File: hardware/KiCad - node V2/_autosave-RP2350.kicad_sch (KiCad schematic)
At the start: 91 parts, among them J3 USB_C_Receptacle_USB2.0_14P, SW1 BOOTSEL, U1 RP2350A, U2 THVD1450D, U3 ADXL355BEZ, U4 TPS2121RUXR, U5 USBLC6-2SC6, U6 TLV75733PDBV, U7 W25Q128JVS, U8 TPS7A20xxxDBV

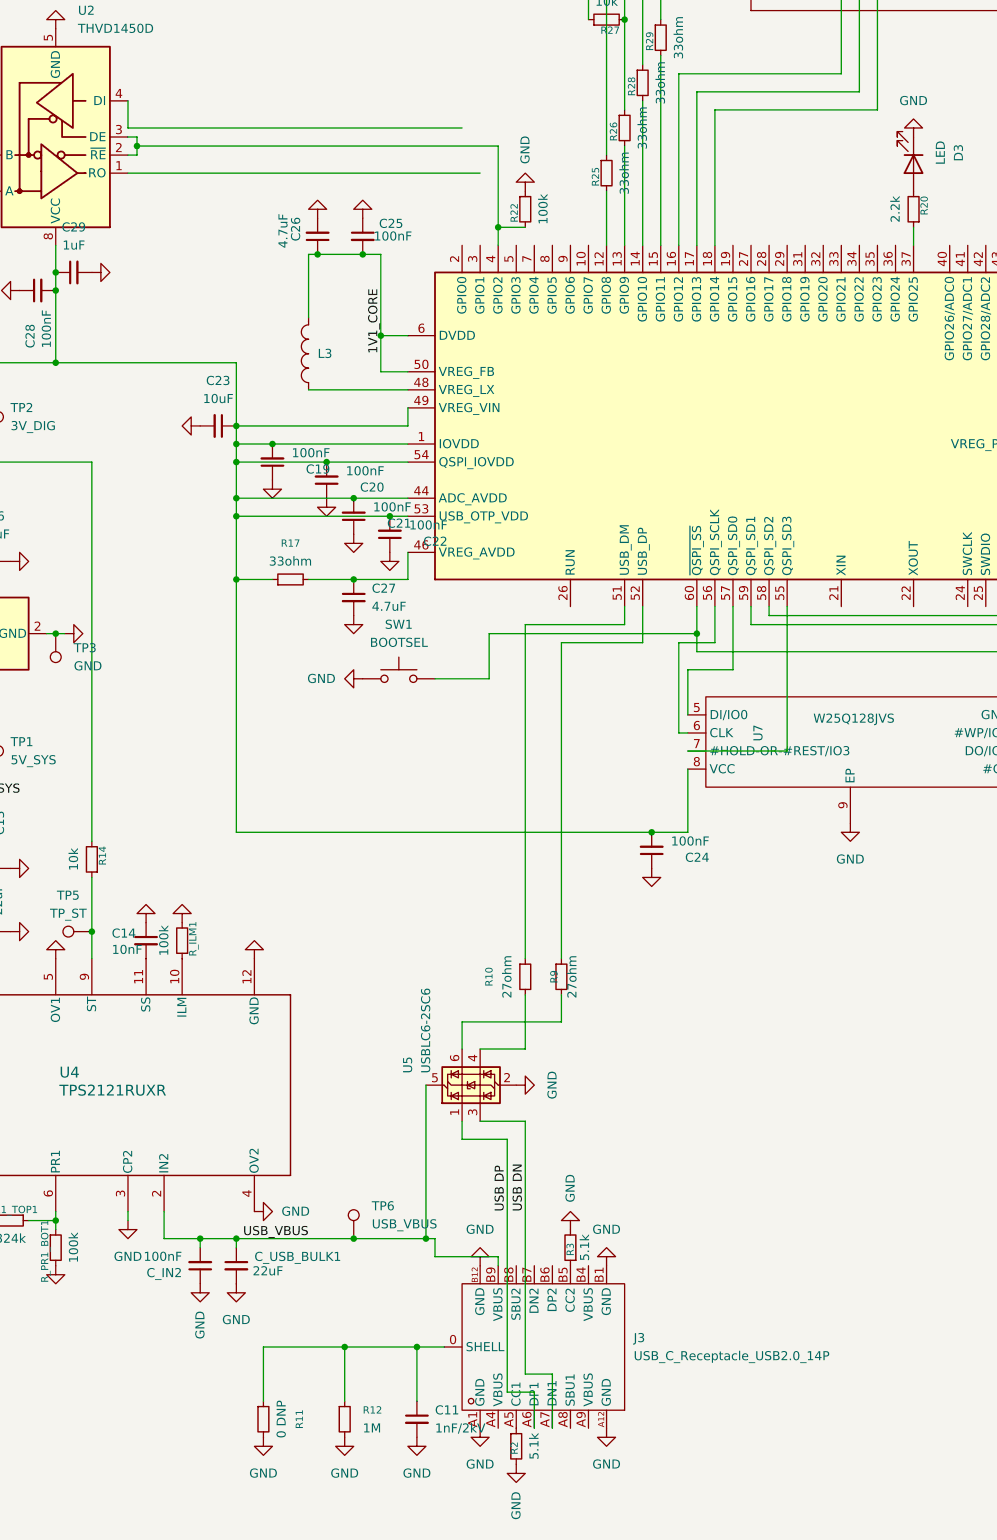
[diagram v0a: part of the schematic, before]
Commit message: hardware: 3v3_dig, 1vcore
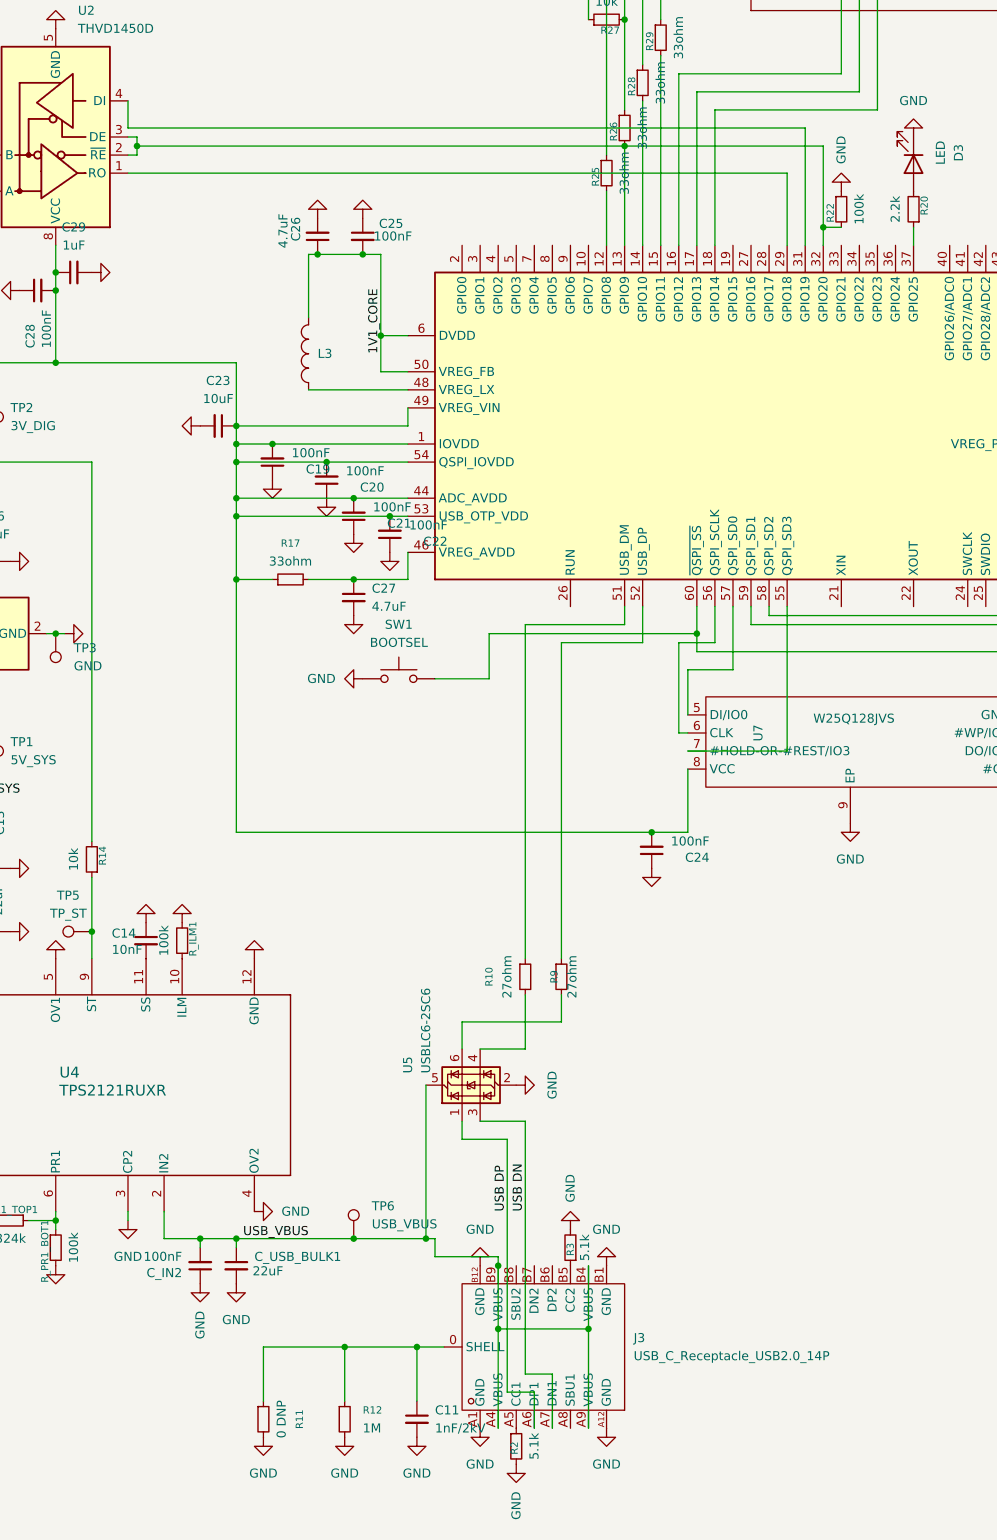
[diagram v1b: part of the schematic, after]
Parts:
- C19, C20, C21, C22, C25: footprint Capacitor_SMD:C_0603_1608Metric -> Capacitor_SMD:C_0402_1005Metric
- C23, C26: footprint Capacitor_SMD:C_0805_2012Metric -> Capacitor_SMD:C_0603_1608Metric
- R17: footprint Resistor_SMD:R_0201_0603Metric -> Resistor_SMD:R_0402_1005Metric
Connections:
- net USB_VBUS: now also J3.A4 (VBUS), J3.A9 (VBUS), J3.B4 (VBUS)
- net at U2.1 (RO): now also U1.29 (GPIO18)
- net at R22.2, U2.2 (~{RE}), U2.3 (DE): now also R26.2, U1.13 (GPIO9), U1.32 (GPIO20); no longer U1.4 (GPIO2)
- net at U2.4 (DI): now also U1.31 (GPIO19)
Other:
- moved on the sheet: R22
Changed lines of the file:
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@@
 	)
 	(junction
+		(at 186.69 241.3)
+		(diameter 0)
+		(color 0 0 0 0)
+	)
+	(junction
 		(at 137.16 228.6)
 		(diameter 0)
@@
 	)
 	(junction
+		(at 173.99 232.41)
+		(diameter 0)
+		(color 0 0 0 0)
+	)
+	(junction
+		(at 219.71 86.36)
+		(diameter 0)
+		(color 0 0 0 0)
+	)
+	(junction
 		(at 100.33 113.03)
 		(diameter 0)
@@
 	)
 	(junction
-		(at 173.99 86.36)
-		(diameter 0)
-		(color 0 0 0 0)
-	)
-	(junction
 		(at 66.04 34.29)
 		(diameter 0)
@@
 	)
 	(junction
+		(at 173.99 241.3)
+		(diameter 0)
+		(color 0 0 0 0)
+	)
+	(junction
 		(at 46.99 237.49)
 		(diameter 0)
@@
 	)
 	(junction
+		(at 191.77 74.93)
+		(diameter 0)
+		(color 0 0 0 0)
+	)
+	(junction
 		(at 137.16 127)
 		(diameter 0)
@@
 	(wire
 		(pts
+			(xy 186.69 255.27) (xy 186.69 241.3)
+		)
+		(stroke
+			(width 0)
+			(type default)
+		)
+	)
+	(wire
+		(pts
 			(xy 196.85 31.75) (xy 196.85 34.29)
 		)
@@
 	(wire
 		(pts
+			(xy 219.71 74.93) (xy 219.71 86.36)
+		)
+		(stroke
+			(width 0)
+			(type default)
+		)
+	)
+	(wire
+		(pts
 			(xy 194.31 88.9) (xy 194.31 68.58)
 		)
@@
 	(wire
 		(pts
+			(xy 219.71 86.36) (xy 222.25 86.36)
+		)
+		(stroke
+			(width 0)
+			(type default)
+		)
+	)
+	(wire
+		(pts
+			(xy 214.63 78.74) (xy 214.63 88.9)
+		)
+		(stroke
+			(width 0)
+			(type default)
+		)
+	)
+	(wire
+		(pts
 			(xy 201.93 40.64) (xy 198.12 40.64)
 		)
@@
 	(wire
 		(pts
+			(xy 186.69 232.41) (xy 186.69 241.3)
+		)
+		(stroke
+			(width 0)
+			(type default)
+		)
+	)
+	(wire
+		(pts
 			(xy 123.19 76.2) (xy 121.92 76.2)
 		)
@@
 	(wire
 		(pts
+			(xy 191.77 74.93) (xy 219.71 74.93)
+		)
+		(stroke
+			(width 0)
+			(type default)
+		)
+	)
+	(wire
+		(pts
 			(xy 22.86 204.47) (xy 22.86 214.63)
 		)
@@
 	(wire
 		(pts
-			(xy 121.92 72.39) (xy 168.91 72.39)
+			(xy 121.92 72.39) (xy 217.17 72.39)
 		)
 		(stroke
@@
 	(wire
 		(pts
-			(xy 52.07 142.24) (xy 52.07 157.48)
+			(xy 173.99 232.41) (xy 173.99 241.3)
 		)
 		(stroke
@@
 	(wire
 		(pts
-			(xy 177.8 142.24) (xy 177.8 189.23)
+			(xy 52.07 142.24) (xy 52.07 157.48)
 		)
 		(stroke
@@
 	(wire
 		(pts
-			(xy 111.76 95.25) (xy 111.76 105.41)
+			(xy 177.8 142.24) (xy 177.8 189.23)
 		)
 		(stroke
@@
 	(wire
 		(pts
-			(xy 97.79 72.39) (xy 97.79 78.74)
+			(xy 111.76 95.25) (xy 111.76 105.41)
 		)
 		(stroke
@@
 	(wire
 		(pts
-			(xy 64.77 209.55) (xy 64.77 226.06)
+			(xy 97.79 72.39) (xy 97.79 78.74)
 		)
 		(stroke
@@
 	(wire
 		(pts
-			(xy 137.16 127) (xy 137.16 124.46)
+			(xy 64.77 209.55) (xy 64.77 226.06)
 		)
 		(stroke
@@
 	(wire
 		(pts
-			(xy 52.07 165.1) (xy 49.53 165.1)
+			(xy 137.16 127) (xy 137.16 124.46)
 		)
 		(stroke
@@
 	(wire
 		(pts
-			(xy 173.99 86.36) (xy 177.8 86.36)
+			(xy 52.07 165.1) (xy 49.53 165.1)
 		)
 		(stroke
@@
 	(wire
 		(pts
-			(xy 173.99 86.36) (xy 173.99 88.9)
-		)
-		(stroke
-			(width 0)
-			(type default)
-		)
-	)
-	(wire
-		(pts
 			(xy 182.88 198.12) (xy 182.88 194.31)
 		)
@@
 	(wire
 		(pts
-			(xy 123.19 74.93) (xy 173.99 74.93)
+			(xy 123.19 74.93) (xy 191.77 74.93)
 		)
 		(stroke
@@
 	(wire
 		(pts
-			(xy 173.99 74.93) (xy 173.99 86.36)
-		)
-		(stroke
-			(width 0)
-			(type default)
-		)
-	)
-	(wire
-		(pts
 			(xy 31.75 212.09) (xy 27.94 212.09)
 		)
@@
 	(wire
 		(pts
+			(xy 217.17 72.39) (xy 217.17 88.9)
+		)
+		(stroke
+			(width 0)
+			(type default)
+		)
+	)
+	(wire
+		(pts
 			(xy 100.33 133.35) (xy 100.33 135.89)
 		)
@@
 	(wire
 		(pts
-			(xy 121.92 78.74) (xy 171.45 78.74)
+			(xy 121.92 78.74) (xy 214.63 78.74)
 		)
 		(stroke
@@
 	(wire
 		(pts
+			(xy 173.99 241.3) (xy 173.99 255.27)
+		)
+		(stroke
+			(width 0)
+			(type default)
+		)
+	)
+	(wire
+		(pts
 			(xy 181.61 247.65) (xy 181.61 255.27)
 		)
@@
 	(wire
 		(pts
+			(xy 186.69 241.3) (xy 173.99 241.3)
+		)
+		(stroke
+			(width 0)
+			(type default)
+		)
+	)
+	(wire
+		(pts
 			(xy 209.55 142.24) (xy 255.27 142.24)
 		)
@@
 	(wire
 		(pts
+			(xy 219.71 88.9) (xy 219.71 86.36)
+		)
+		(stroke
+			(width 0)
+			(type default)
+		)
+	)
+	(wire
+		(pts
 			(xy 87.63 83.82) (xy 87.63 90.17)
 		)
@@
 			)
 		)
-		(property "Footprint" "Capacitor_SMD:C_0603_1608Metric"
+		(property "Footprint" "Capacitor_SMD:C_0402_1005Metric"
 			(at 153.67 127 0)
 			(hide yes)
@@
 			)
 		)
-		(property "Footprint" "Capacitor_SMD:C_0805_2012Metric"
+		(property "Footprint" "Capacitor_SMD:C_0603_1608Metric"
 			(at 134.62 114.3 0)
 			(hide yes)
@@
 			)
 		)
-		(property "Footprint" "Capacitor_SMD:C_0603_1608Metric"
+		(property "Footprint" "Capacitor_SMD:C_0402_1005Metric"
 			(at 158.75 129.54 0)
 			(hide yes)
@@
 	(symbol
 		(lib_id "power:GND")
-		(at 177.8 81.28 180)
+		(at 222.25 81.28 180)
 		(unit 1)
 		(body_style 1)
@@
 		(fields_autoplaced yes)
 		(property "Reference" "#PWR049"
-			(at 177.8 74.93 0)
+			(at 222.25 74.93 0)
 			(hide yes)
 			(show_name no)
@@
 		)
 		(property "Value" "GND"
-			(at 177.7999 77.47 90)
+			(at 222.2499 77.47 90)
 			(show_name no)
 			(do_not_autoplace no)
@@
 		)
 		(property "Footprint" ""
-			(at 177.8 81.28 0)
+			(at 222.25 81.28 0)
 			(hide yes)
 			(show_name no)
@@
 		)
 		(property "Datasheet" ""
-			(at 177.8 81.28 0)
+			(at 222.25 81.28 0)
 			(hide yes)
 			(show_name no)
@@
 		)
 		(property "Description" "Power symbol creates a global label with name \"GND\" , ground"
-			(at 177.8 81.28 0)
+			(at 222.25 81.28 0)
 			(hide yes)
 			(show_name no)
@@
 			)
 		)
-		(property "Footprint" "Capacitor_SMD:C_0603_1608Metric"
+		(property "Footprint" "Capacitor_SMD:C_0402_1005Metric"
 			(at 154.94 87.63 0)
 			(hide yes)
@@
 			)
 		)
-		(property "Footprint" "Capacitor_SMD:C_0603_1608Metric"
+		(property "Footprint" "Capacitor_SMD:C_0402_1005Metric"
 			(at 142.24 119.38 0)
 			(hide yes)
@@
 	(symbol
 		(lib_id "Device:R_Small")
-		(at 177.8 83.82 0)
+		(at 222.25 83.82 0)
 		(unit 1)
 		(body_style 1)
@@
 		(dnp no)
 		(property "Reference" "R22"
-			(at 176.276 84.328 90)
+			(at 220.726 84.328 90)
 			(show_name no)
 			(do_not_autoplace no)
@@
 		)
 		(property "Value" "100k"
-			(at 180.34 83.82 90)
+			(at 224.79 83.82 90)
 			(show_name no)
 			(do_not_autoplace no)
@@
 		)
 		(property "Footprint" "Resistor_SMD:R_0603_1608Metric"
-			(at 177.8 83.82 0)
+			(at 222.25 83.82 0)
 			(hide yes)
 			(show_name no)
@@
 		)
 		(property "Datasheet" ""
-			(at 177.8 83.82 0)
+			(at 222.25 83.82 0)
 			(hide yes)
 			(show_name no)
@@
 		)
 		(property "Description" "Resistor, small symbol"
-			(at 177.8 83.82 0)
+			(at 222.25 83.82 0)
 			(hide yes)
 			(show_name no)
@@
 			)
 		)
-		(property "Footprint" "Capacitor_SMD:C_0805_2012Metric"
+		(property "Footprint" "Capacitor_SMD:C_0603_1608Metric"
 			(at 148.59 87.63 0)
 			(hide yes)
@@
 			)
 		)
-		(property "Footprint" "Resistor_SMD:R_0201_0603Metric"
+		(property "Footprint" "Resistor_SMD:R_0402_1005Metric"
 			(at 144.78 135.89 0)
 			(hide yes)
@@
 			)
 		)
-		(property "Footprint" "Capacitor_SMD:C_0603_1608Metric"
+		(property "Footprint" "Capacitor_SMD:C_0402_1005Metric"
 			(at 149.86 121.92 0)
 			(hide yes)

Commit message: hardware: new layout
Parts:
- removed R25, R26, R28, R29: 33ohm, Resistor_SMD:R_0603_1608Metric, symbol Device:R_Small
- C30, C34, C35, C37: footprint Capacitor_SMD:C_0603_1608Metric -> Capacitor_SMD:C_0402_1005Metric
- C36: footprint Capacitor_SMD:C_0805_2012Metric -> Capacitor_SMD:C_0603_1608Metric
- R23, R24, R27: footprint Resistor_SMD:R_0603_1608Metric -> Resistor_SMD:R_0402_1005Metric
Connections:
- net GND: now also J_OUT1.2 (GND)
- net SHIELD: now also J_OUT1.5 (SHIELD)
- net at U2.1 (RO): now also U1.27 (GPIO16); no longer U1.29 (GPIO18)
- net at R22.2, U2.2 (~{RE}), U2.3 (DE): now also U1.29 (GPIO18); no longer U1.13 (GPIO9), U1.32 (GPIO20)
- net at U2.4 (DI): now also U1.28 (GPIO17); no longer U1.31 (GPIO19)
- net ADXL_MISO: now reaches U3.4 (MISO/ASEL)
- net ADXL_MISO: now also U1.12 (GPIO8)
- net ADXL_CS: now reaches R27.2, U3.1 (*CS/SCL)
- net ADXL_CS: now also U1.13 (GPIO9)
- net ADXL_INT1: now reaches U3.12 (INT1)
- net ADXL_INT1: now also U1.18 (GPIO14); no longer U1.17 (GPIO13)
- net ADXL_INT2: now reaches U3.13 (INT2)
- net ADXL_INT2: now also U1.17 (GPIO13); no longer U1.18 (GPIO14)
- net ADXL_DRDY: now reaches U1.16 (GPIO12), U3.14 (DRDY)
- net ADXL_SCLK: now reaches U3.2 (SCLK/VSSIO)
- net ADXL_SCLK: now also U1.14 (GPIO10)
- net ADXL_MOSI: now reaches U3.3 (MOSI/SDA)
- net ADXL_MOSI: now also U1.15 (GPIO11)
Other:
- moved on the sheet: R22, R27
